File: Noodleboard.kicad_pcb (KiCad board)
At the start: 2 copper layers, 50 x 50 mm, 60 parts, among them CON1 SWD, IC1 LD1117S33, IC3 USBLC6-4, IC5 USB3300, P1 MICROUSBAB, Q1 BC850, SW2 SW_PUSH, U1 STM32F405RGT6, U2 ARDUINO_UNO_EX, X1 25 MHz

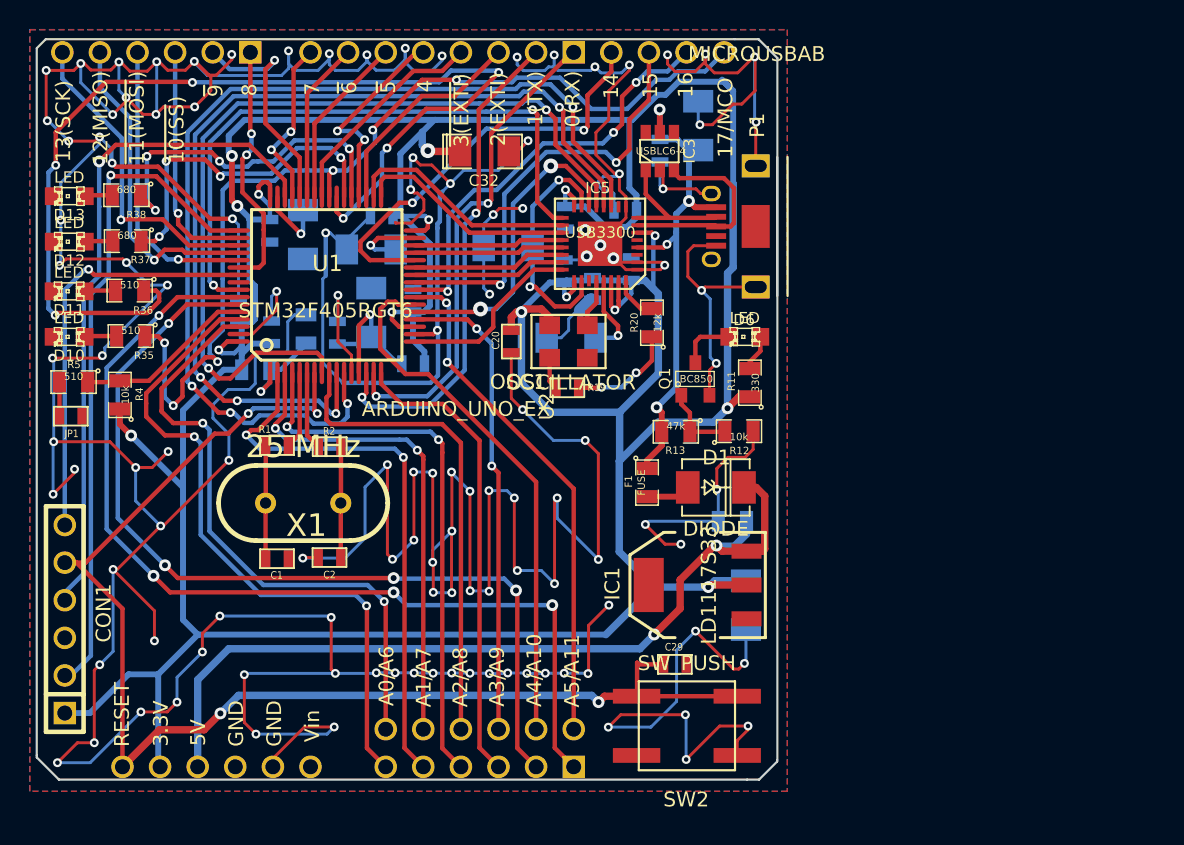
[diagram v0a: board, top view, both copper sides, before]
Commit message: - New PCB design  - Updated last schematics modifications  - Added Gerber outputs (old and new version)
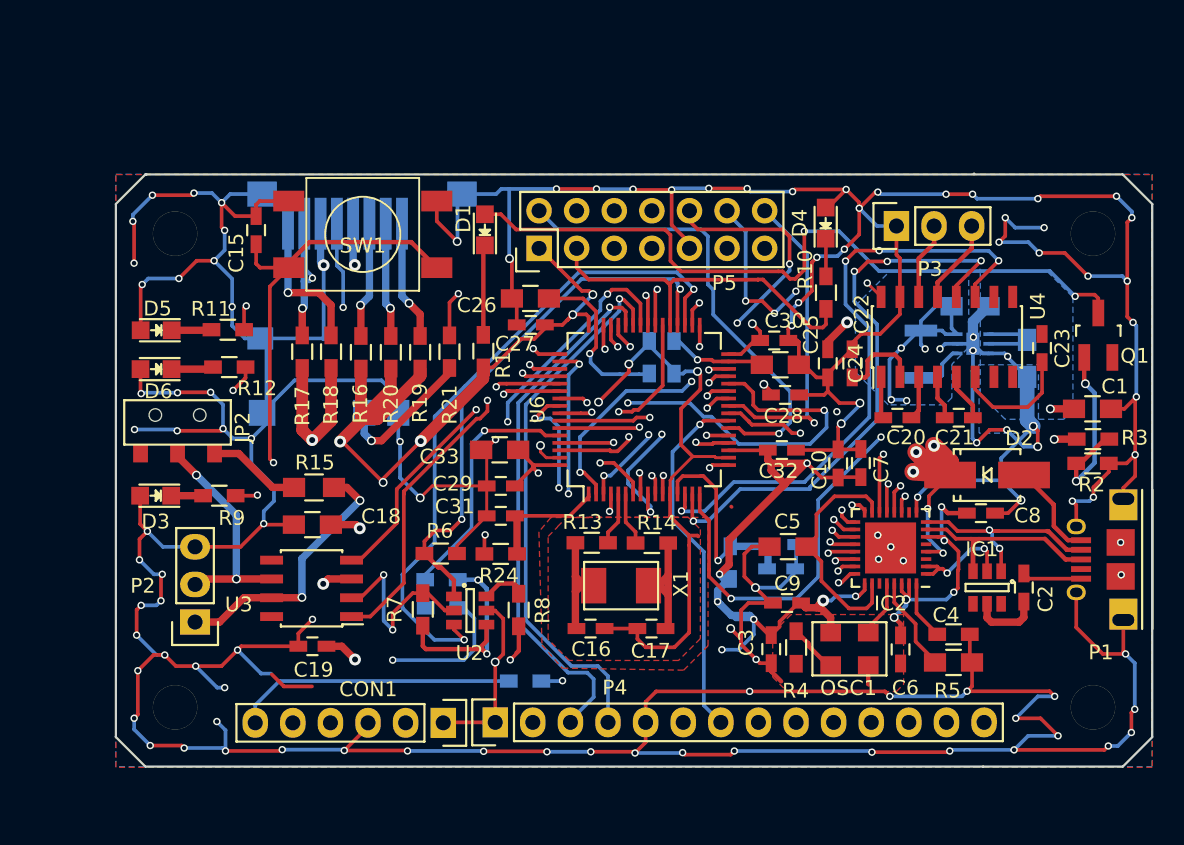
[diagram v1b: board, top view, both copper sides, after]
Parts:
- removed D10, D11, D12, D13: LED, LED-0805
- removed F1: FUSE, SM0805
- removed IC3: USBLC6-4, SOT23_6
- removed IC5: USB3300, QFN32
- removed R35, R36: 510, SM0805
- removed R37, R38: 680, SM0805
- removed SW2: SW_PUSH, EVQP0
- added C16: 4.7p, Capacitors_SMD:C_0603_HandSoldering, F.Cu at (152.1, 110.7)
- added C17: 4.7p, Capacitors_SMD:C_0603_HandSoldering, F.Cu at (156.2, 110.7)
- added C24: 1u, Capacitors_SMD:C_0603_HandSoldering, F.Cu at (168.1, 92.8)
- added C25: 2u2, Capacitors_SMD:C_0805_HandSoldering, F.Cu at (164.9, 92.9)
- added C28: 100n, Capacitors_SMD:C_0603_HandSoldering, F.Cu at (165.2, 94.9)
- added C30: 100n, Capacitors_SMD:C_0603_HandSoldering, F.Cu at (164.5, 91.2)
- added C31: 1u, Capacitors_SMD:C_0603_HandSoldering, F.Cu at (146.0, 103.1)
- added D2: D, Diodes_SMD:SMA_Handsoldering, F.Cu at (178.8, 100.3)
- added D3: LED, LEDs:LED-0805, F.Cu at (122.7, 101.7)
- added D4: LED, LEDs:LED-0805, F.Cu at (167.9, 83.3)
- added D5: LED, LEDs:LED-0805, F.Cu at (122.7, 90.5)
- added Hole3mm: VAL**, ComponentLib:Hole3mm, F.Cu at (128.2, 87.9)
- added Hole3mm: VAL**, ComponentLib:Hole3mm, F.Cu at (186.0, 83.7)
- added Hole3mm: VAL**, ComponentLib:Hole3mm, F.Cu at (186.1, 116.9)
- added Hole3mm: VAL**, ComponentLib:Hole3mm, F.Cu at (124.1, 116.6)
- added IC2: USB3300, Housings_DFN_QFN:QFN-32-1EP_5x5mm_Pitch0.5mm, F.Cu at (172.3, 105.2)
- added JP2: Jumper_NC_Small, ComponentLibv2:AYZ-SlideSwitches, F.Cu at (124.2, 98.9)
- added JP3: Jumper_NO_Small, Resistors_SMD:R_0603_HandSoldering, B.Cu at (156.0, 92.3)
- added JP4: Jumper_NO_Small, Resistors_SMD:R_0603_HandSoldering, B.Cu at (157.7, 92.4)
- added L2: fcm1608, Resistors_SMD:R_0603_HandSoldering, B.Cu at (161.5, 106.2)
- added P2: CONN_01X03, Pin_Headers:Pin_Header_Straight_1x03, F.Cu at (125.3, 110.2)
- added P3: CONN_01X03, Pin_Headers:Pin_Header_Straight_1x03, F.Cu at (172.7, 83.5)
- added P4: CONN_01X14, Pin_Headers:Pin_Header_Straight_1x14, F.Cu at (145.6, 117.0)
- added P5: CONN_02X07, Pin_Headers:Pin_Header_Straight_2x07, F.Cu at (148.6, 85.0)
- added R10: 510, Resistors_SMD:R_0603_HandSoldering, F.Cu at (168.0, 88.0)
- added R14: 0, Resistors_SMD:R_0603_HandSoldering, F.Cu at (156.2, 104.9)
- added R15: 120, Resistors_SMD:R_0805_HandSoldering, F.Cu at (133.4, 101.1)
- added R16: 47K, Resistors_SMD:R_0603_HandSoldering, F.Cu at (136.6, 92.0)
- added R17: 47K, Resistors_SMD:R_0603_HandSoldering, F.Cu at (132.6, 92.0)
- added R18: 47K, Resistors_SMD:R_0603_HandSoldering, F.Cu at (134.5, 92.0)
- added R21: 0, Resistors_SMD:R_0603_HandSoldering, F.Cu at (142.5, 92.0)
- added R22: 0, Resistors_SMD:R_0603_HandSoldering, B.Cu at (142.0, 107.4)
- added R23: 1K, Resistors_SMD:R_0603_HandSoldering, B.Cu at (142.0, 109.3)
- added R24: 47, Resistors_SMD:R_0603_HandSoldering, F.Cu at (146.0, 105.6)
- added R6: 47k, Resistors_SMD:R_0603_HandSoldering, F.Cu at (141.9, 105.6)
- added R7: 47k, Resistors_SMD:R_0603_HandSoldering, F.Cu at (140.7, 109.4)
- added R8: 47k, Resistors_SMD:R_0603_HandSoldering, F.Cu at (147.2, 109.4)
- added R9: 510, Resistors_SMD:R_0603_HandSoldering, F.Cu at (127.0, 101.7)
- added SW1: SW_PUSH, ComponentLib:SW_PUSH_SMALL_SMD, F.Cu at (136.7, 84.0)
- added U3: SN65HVD232, Housings_SOIC:SOIC-8_3.9x4.9mm_Pitch1.27mm, F.Cu at (133.2, 108.0)
- added U4: MAX232, Housings_SOIC:SOIC-16_3.9x9.9mm_Pitch1.27mm, F.Cu at (176.1, 91.0)
- added U5: SD_CARD, ComponentLibv2:uSDCard, B.Cu at (136.6, 89.1)
- added U6: STM32F405RGT6, Housings_QFP:LQFP-64_10x10mm_Pitch0.5mm, F.Cu at (155.7, 95.9)
- C1: value 4.7p -> 4u7; footprint SM0603 -> Capacitors_SMD:C_0805_HandSoldering
- C10: value 2u2 -> 100n; footprint SM1206POL -> Capacitors_SMD:C_0603_HandSoldering; moved to F.Cu
- C11: value 100n -> 4u7; footprint SM0603 -> Capacitors_SMD:C_0805_HandSoldering
- C12: value 2u2 -> 10u; footprint SM1206POL -> Capacitors_SMD:C_0805_HandSoldering
- C13: footprint SM0805 -> Capacitors_SMD:C_0603_HandSoldering
- C14: value 10u -> 100n; footprint SM1206POL -> Capacitors_SMD:C_0603_HandSoldering
- C15, C19, C27, C7, C8, C9: footprint SM0603 -> Capacitors_SMD:C_0603_HandSoldering; moved to F.Cu
- C18: value 4u7 -> 10u; footprint SM1206POL -> Capacitors_SMD:C_0805_HandSoldering; moved to F.Cu
- C2: value 4.7p -> 100n; footprint SM0603 -> Capacitors_SMD:C_0603_HandSoldering
- C20: value 100n -> 1u; footprint SM0603 -> Capacitors_SMD:C_0603_HandSoldering
- C21, C22: value 4u7 -> 1u; footprint SM1206POL -> Capacitors_SMD:C_0603_HandSoldering; moved to F.Cu
- C23: value 100n -> 1u; footprint SM0603 -> Capacitors_SMD:C_0603_HandSoldering; moved to F.Cu
- C26: value 100n -> 2u2; footprint SM0603 -> Capacitors_SMD:C_0805_HandSoldering; moved to F.Cu
- C29: footprint SM0603 -> Capacitors_SMD:C_0603_HandSoldering
- C3: value 1u -> 100n; footprint SM1206POL -> Capacitors_SMD:C_0603_HandSoldering; moved to F.Cu
- C32: value 4u7 -> 100n; footprint SM1206POL -> Capacitors_SMD:C_0603_HandSoldering
- C33, C4, C5: value 100n -> 4u7; footprint SM0603 -> Capacitors_SMD:C_0805_HandSoldering; moved to F.Cu
- C6: value 1u -> 100n; footprint SM0805 -> Capacitors_SMD:C_0603_HandSoldering; moved to F.Cu
- CON1: footprint PIN_ARRAY-6X1 -> Pin_Headers:Pin_Header_Straight_1x06
- D1: value DIODE -> LED; footprint DO-214AC(SMA) -> LEDs:LED-0805
- D6: footprint LED-0805 -> LEDs:LED-0805
- IC1: value LD1117S33 -> USBLC6-4; footprint SOT223 -> TO_SOT_Packages_SMD:SOT-23-6
- JP1: value JUMPER -> Jumper_NO_Small; footprint SM0603 -> Resistors_SMD:R_0603_HandSoldering; moved to B.Cu
- L1: value fcm1608 -> 2u2; footprint SM0603 -> ComponentLibv2:SMD_1008
- OSC1: footprint 26MHZOSC -> ComponentLib:26MHZOSC
- P1: footprint microUSB-AB -> ComponentLibv2:uUSB-AB
- Q1: footprint SOT23 -> TO_SOT_Packages_SMD:SOT-23_Handsoldering
- R1: value 0 -> 330; footprint SM0603 -> Resistors_SMD:R_0603_HandSoldering
- R11: value 330 -> 510; footprint SM0805 -> Resistors_SMD:R_0603_HandSoldering
- R12: value 10k -> 510; footprint SM0805 -> Resistors_SMD:R_0603_HandSoldering
- R13: value 47k -> 0; footprint SM0805 -> Resistors_SMD:R_0603_HandSoldering
- R19: value NP -> 47K; footprint SM0603 -> Resistors_SMD:R_0603_HandSoldering
- R2: value 0 -> 10k; footprint SM0603 -> Resistors_SMD:R_0603_HandSoldering
- R20: value 12k -> 47K; footprint SM0805 -> Resistors_SMD:R_0603_HandSoldering
- R3: value 47 -> 47k; footprint SM0805 -> Resistors_SMD:R_0603_HandSoldering; moved to F.Cu
- R4: value 10k -> NP; footprint SM0805 -> Resistors_SMD:R_0603_HandSoldering
- R5: value 510 -> 12k; footprint SM0805 -> Resistors_SMD:R_0603_HandSoldering
- U1: value STM32F405RGT6 -> TPS62291DRVT; footprint LQFP64 -> ComponentLibv2:S-PWSON-N6; moved to B.Cu
- U2: value ARDUINO_UNO_EX -> SN74LVC1G373; footprint ArduinoUNOShieldEX -> TO_SOT_Packages_SMD:SOT-23-6
- X1: footprint HC-49V -> ComponentLibv2:7A-25.000MAAJ-T
- moved R5 61.8 mm to (176.6, 111.1)
- moved R3 56.7 mm to (186.0, 97.9), turned to 180 degrees
- moved C1 56.0 mm to (186.0, 95.8), turned to 0 degrees
- moved C11 51.9 mm to (181.6, 92.4), turned to 270 degrees
- moved R2 51.5 mm to (186.0, 99.5), turned to 0 degrees
- moved R4 48.8 mm to (165.9, 112.0), turned to 270 degrees
- moved C4 47.2 mm to (176.6, 113.0), turned to 0 degrees
- moved C2 46.9 mm to (181.3, 107.9), turned to 270 degrees
- moved C6 45.6 mm to (173.0, 112.1), turned to 270 degrees
- moved C12 45.3 mm to (177.7, 88.9), turned to 0 degrees
- moved U1 43.9 mm to (177.9, 91.4), turned to 90 degrees
- moved C7 43.3 mm to (170.3, 99.5), turned to 90 degrees
- moved C8 41.0 mm to (178.4, 102.9), turned to 0 degrees
- moved C19 40.9 mm to (133.3, 111.9), turned to 180 degrees
- moved D6 39.8 mm to (122.7, 93.2)
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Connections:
- C1 pad 1: GND -> /B2B/5V0
- C1 pad 2: N-0000049 -> GND
- C10 pad 1: /VCAP_1 -> /B2B/3V3
- C11 pad 1: GND -> /B2B/5V0
- C11 pad 2: /USB/3V30 -> GND
- C12 pad 1: /VCAP_2 -> /B2B/3V3
- C13 pad 1: /Peripherals/5V -> /MCU/VDDA
- C14 pad 1: /USB/3V30 -> /MCU/VDDA
- C15 pad 1: /USB/3V30 -> /Boot/~RST
- C18 pad 1: /USB/VBUS_HS_0 -> /B2B/3V3
- C19 pad 1: GND -> /B2B/3V3
- C19 pad 2: /USB/VBUS_HS_0 -> GND
- C2 pad 2: N-0000048 -> /USB/VBUS_HS
- C20 pad 1: /USB/3V30 -> Net-(C20-Pad1)
- C20 pad 2: GND -> Net-(C20-Pad2)
- C21 pad 2: GND -> Net-(C21-Pad2)
- C22 pad 1: N-0000072 -> GND
- C22 pad 2: GND -> Net-(C22-Pad2)
- C23 pad 1: /USB/3V30 -> GND
- C23 pad 2: GND -> Net-(C23-Pad2)
- C26 pad 1: /USB/3V30 -> /MCU/VCAP_2
- C27 pad 1: /USB/3V30 -> GND
- C27 pad 2: GND -> /B2B/3V3
- C29 pad 1: /Peripherals/RESET_BUTTON -> GND
- C29 pad 2: GND -> /B2B/3V3
- C3 pad 1: /VDDA -> /B2B/3V3
- C32 pad 1: /USB/3V30 -> GND
- C32 pad 2: GND -> /B2B/3V3
- C33 pad 1: /USB/3V30 -> /B2B/3V3
- C4 pad 1: /VDDA -> Net-(C4-Pad1)
- C5 pad 1: /USB/3V30 -> Net-(C5-Pad1)
- C6 pad 1: /VBAT -> /B2B/3V3
- C7 pad 1: GND -> /B2B/3V3
- C7 pad 2: /USB/3V30 -> GND
- C8 pad 1: GND -> /B2B/3V3
- C8 pad 2: /USB/3V30 -> GND
- C9 pad 1: GND -> /B2B/3V3
- C9 pad 2: /USB/3V30 -> GND
- CON1 pad 1: /USB/3V30 -> /B2B/3V3
- CON1 pad 2: /SWCLK -> /Debug/SWCLK
- CON1 pad 4: /SWDIO -> /Debug/SWDIO
- CON1 pad 5: /Peripherals/RESET_BUTTON -> /Boot/~RST
- CON1 pad 6: /SWO -> Net-(CON1-Pad6)
- D1 pad 1: N-000001 -> Net-(D1-Pad1)
- D1 pad 2: /Peripherals/5V -> Net-(D1-Pad2)
- D6 pad 1: N-0000081 -> Net-(D6-Pad1)
- D6 pad 2: N-0000075 -> GND
- IC1 pad 1: GND -> /USB/USB_D-
- IC1 pad 2: /USB/3V30 -> GND
- IC1 pad 3: /Peripherals/5V -> /USB/USB_D+
- IC1 pad 4: (no net) -> Net-(IC1-Pad4)
- JP1 pad 1: N-0000032 -> Net-(CON1-Pad6)
- JP1 pad 2: GND -> /B2B/SPI_SCK
- L1 pad 1: /USB/3V30 -> Net-(L1-Pad1)
- L1 pad 2: /VDDA -> /B2B/3V3
- OSC1 pad 1: N-0000077 -> Net-(OSC1-Pad1)
- OSC1 pad 4: /USB/3V30 -> /B2B/3V3
- P1 pad 1: /USB/VBUS_HS_0 -> Net-(D2-Pad2)
- P1 pad 2: N-0000078 -> /USB/USB_D-
- P1 pad 3: N-0000079 -> /USB/USB_D+
- P1 pad 4: (no net) -> Net-(P1-Pad4)
- Q1 pad 1: N-0000073 -> Net-(Q1-Pad1)
- Q1 pad 3: N-0000075 -> Net-(D1-Pad2)
- R1 pad 1: N-0000049 -> /B2B/3V3
- R1 pad 2: /OSC_IN -> Net-(D1-Pad1)
- R11 pad 1: /USB/3V30 -> /IO/LED3
- R11 pad 2: N-0000081 -> Net-(D5-Pad1)
- R12 pad 1: N-0000073 -> /IO/LED4
- R12 pad 2: GND -> Net-(D6-Pad1)
- R13 pad 1: N-0000073 -> Net-(C16-Pad2)
- R13 pad 2: /USB/VBUS_HS_0 -> /Clocks/OSC_IN
- R19 pad 1: N-0000077 -> /MCU/SDIO_D2
- R19 pad 2: GND -> /B2B/3V3
- R2 pad 1: N-0000048 -> Net-(Q1-Pad1)
- R2 pad 2: /OSC_OUT -> GND
- R20 pad 1: GND -> /MCU/SDIO_D3
- R20 pad 2: N-0000074 -> /B2B/3V3
- R3 pad 1: /USB/3V30 -> Net-(Q1-Pad1)
- R3 pad 2: /VBAT -> /B2B/5V0
- R4 pad 1: /USB/3V30 -> Net-(OSC1-Pad1)
- R4 pad 2: /BOOT -> GND
- R5 pad 1: /BOOT -> GND
- R5 pad 2: N-0000032 -> Net-(IC2-Pad32)
- U1 pad 1: /VBAT -> Net-(L1-Pad1)
- U1 pad 2: /Peripherals/A1 -> GND
- U1 pad 3: /Peripherals/A7 -> /B2B/3V3
- U1 pad 4: /Peripherals/A2 -> /B2B/5V0
- U1 pad 5: /OSC_IN -> /B2B/5V0
- U1 pad 6: /OSC_OUT -> GND
- U2 pad 1: /Peripherals/UART_TX -> /Boot/ENABLE_BOOT
- U2 pad 2: /Peripherals/GPIO4 -> GND
- U2 pad 3: /Peripherals/PWM4 -> /Boot/BOOT_STATE
- U2 pad 4: /Peripherals/GPIO3 -> /Boot/BOOT
- U2 pad 5: /Peripherals/PWM3 -> /B2B/3V3
- U2 pad 6: /Peripherals/PWM2 -> Net-(R8-Pad1)
- X1 pad 1: N-0000048 -> Net-(C17-Pad2)
- X1 pad 2: N-0000049 -> Net-(C16-Pad2)
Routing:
- net /USB/3V30: track 298.4 -> 0.00 mm, vias 15 -> 0
- net /B2B/3V3: track 0.00 -> 224.4 mm, vias 0 -> 33
- net /Peripherals/RESET_BUTTON: track 88.2 -> 0.00 mm, vias 4 -> 0
- net /B2B/5V0: track 0.00 -> 76.9 mm, vias 0 -> 12
- net /Boot/~RST: track 0.00 -> 72.8 mm, vias 0 -> 2
- net /Peripherals/LED2: track 71.0 -> 0.00 mm, vias 6 -> 0
- net /Peripherals/LED1: track 65.5 -> 0.00 mm, vias 6 -> 0
- net /Peripherals/SCL: track 65.5 -> 0.00 mm, vias 4 -> 0
- net /Peripherals/SDA: track 61.3 -> 0.00 mm, vias 4 -> 0
- net /IO/LED4: track 0.00 -> 59.9 mm, vias 0 -> 2
- net /Peripherals/5V: track 58.4 -> 0.00 mm, vias 2 -> 0
- net /B2B/DAC: track 0.00 -> 51.0 mm, vias 0 -> 1
- net Net-(D1-Pad2): track 0.00 -> 50.4 mm, vias 0 -> 2
- net /USB/NXT: track 68.4 -> 19.4 mm, vias 4 -> 2
- net /IO/LED3: track 0.00 -> 46.4 mm, vias 0 -> 2
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- added copper zone on F.Cu, net (none)
- added copper zone on B.Cu, net /B2B/3V3
- added copper zone on In2.Cu, net /B2B/3V3
- added copper zone on B.Cu, net /B2B/5V0
- added copper zone on In2.Cu, net /B2B/5V0
- added copper zone on In1.Cu, net GND
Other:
- board size 50 x 50 mm -> 70 x 40.1 mm
- copper layers 2 -> 4
- net class Default: clearance 0.15 -> 0.2; trace_width 0.2 -> 0.25; via_drill 0.3 -> 0.4
- rule pad_to_mask_clearance: 0 -> 0.2
- rule trace_clearance: 0.15 -> 0.2
- rule via_min_drill: 0.3 -> 0.15
- rule via_min_size: 0.6 -> 0.25
- board text added: "Noodleboard - 1.0.0 github.com/javifercep/Noodleboard"
- board text removed: "SBA-COMCenter v0.0 Javier Fernández Cepeda"

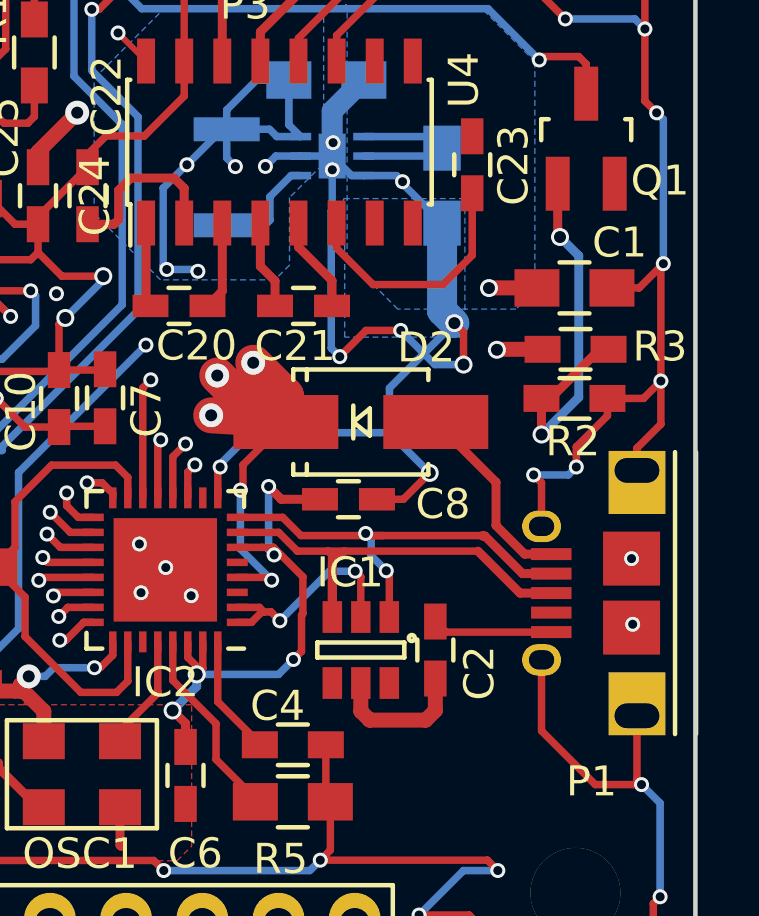
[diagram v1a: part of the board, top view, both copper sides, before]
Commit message: #5 Review USB power supply #6 Power signaling LED should be in power sheet - Simplified outputs (Gerber, sch & pcb)
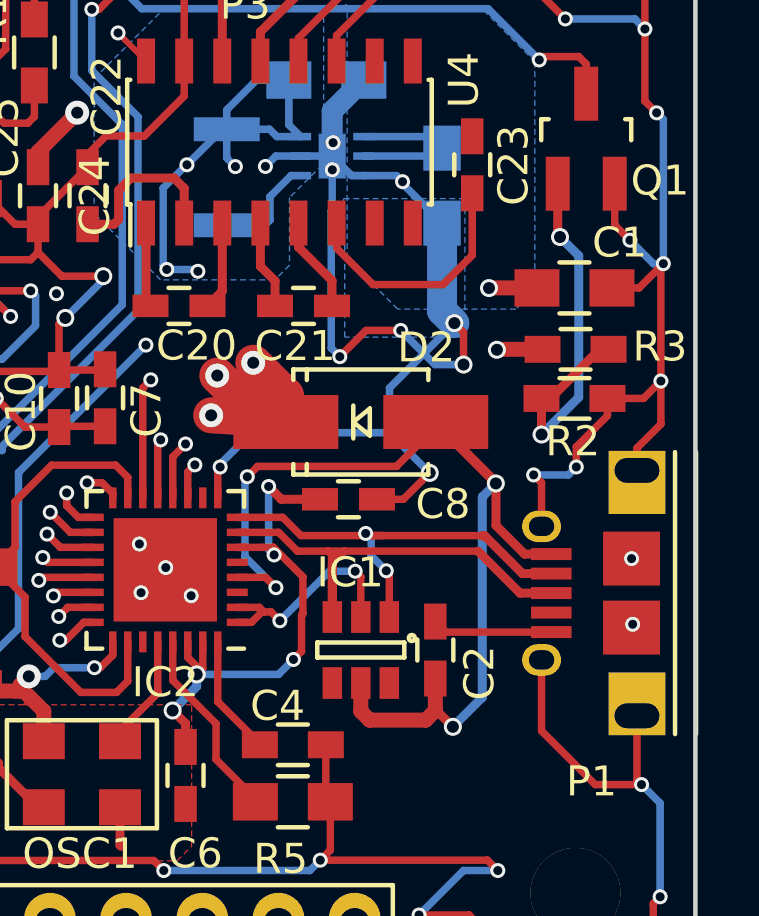
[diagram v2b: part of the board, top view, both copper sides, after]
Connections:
- C2 pad 2: /USB/VBUS_HS -> /USB/VUSB_5V0_I
- D2 pad 2: Net-(D2-Pad2) -> /USB/VUSB_5V0_I
- IC1 pad 5: /USB/VBUS_HS -> /USB/VUSB_5V0_I
- IC2 pad 4: /B2B/5V0 -> /USB/VUSB_5V0_I
- P1 pad 1: Net-(D2-Pad2) -> /USB/VUSB_5V0_I
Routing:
- net /USB/VUSB_5V0_I: track 0.00 -> 36.4 mm, vias 0 -> 4
- net /B2B/5V0: track 76.9 -> 69.4 mm, vias 12 -> 10
- net Net-(D2-Pad2): track 6.52 -> 0.00 mm
- net /USB/VBUS_HS: track 4.75 -> 0.00 mm
- net GND: track 620.6 -> 624.1 mm, vias 124 -> 125
